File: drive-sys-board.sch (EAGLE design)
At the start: 30 parts, among them J2 APP_2POS_CONFIG12V_HORIZ, U1 OKI-78SR-5/1.5-W36HC, U2 MAX232, U3 MAX232, U4 MAX232

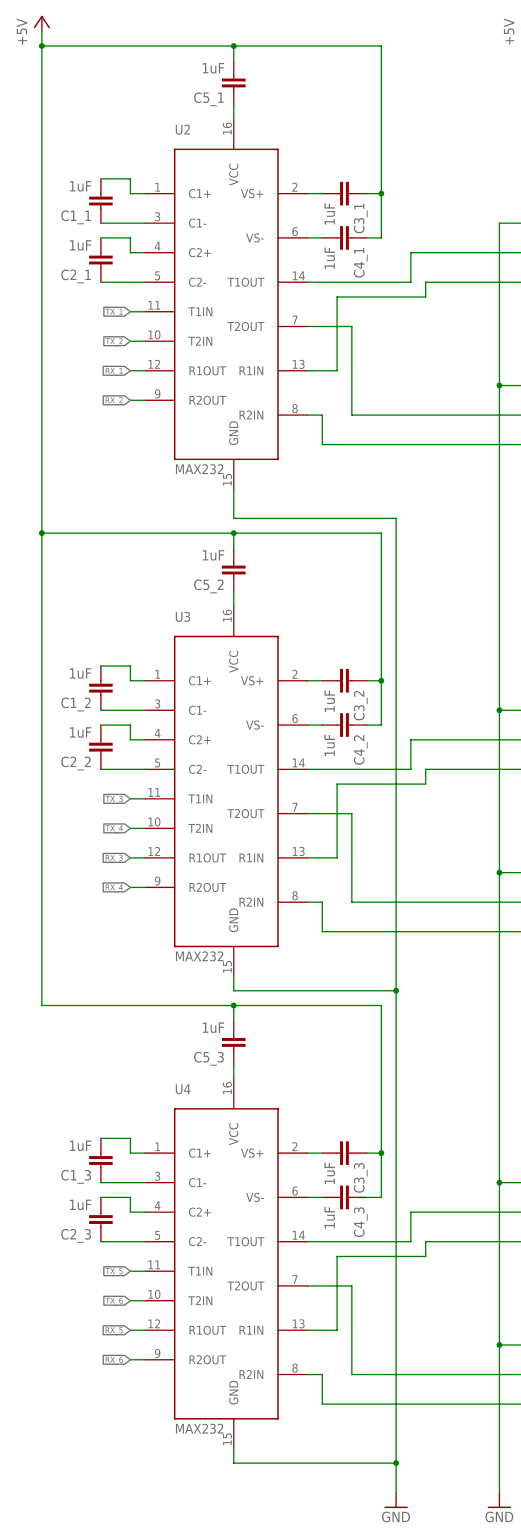
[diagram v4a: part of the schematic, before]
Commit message: Fixed RS232 chip capacitors
Several capacitors were going to Vcc when they should have been going to
Gnd
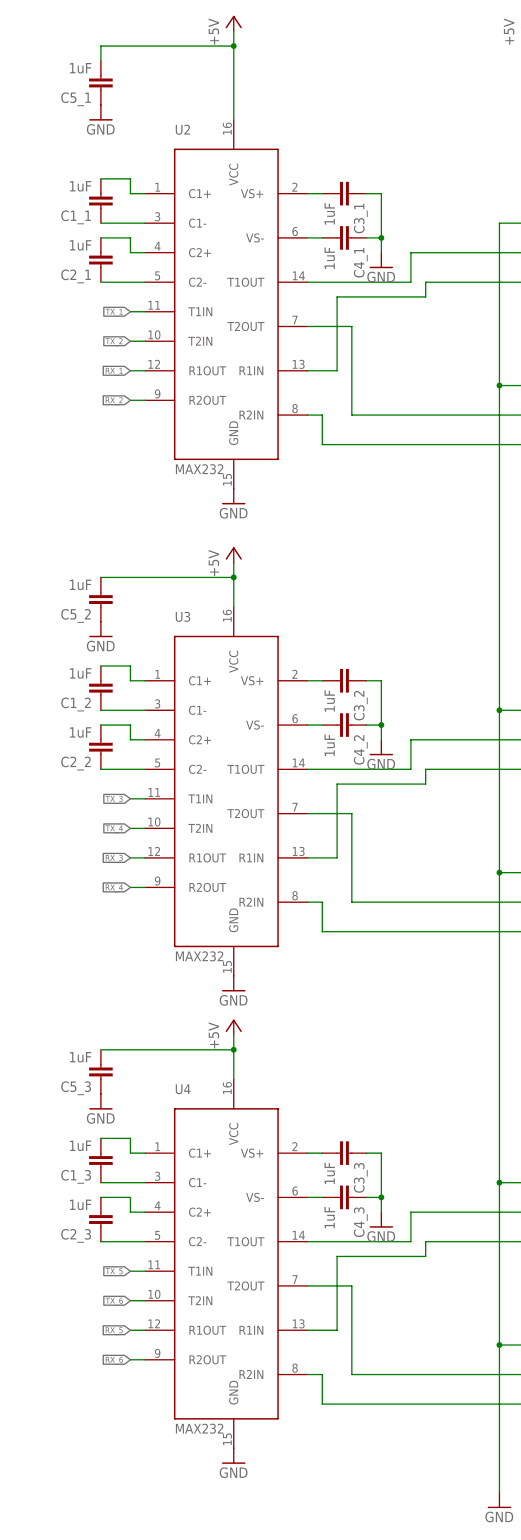
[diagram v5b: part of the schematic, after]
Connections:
- removed net N$10: C5_1.1, U2.VCC
- removed net N$17: C5_2.1, U3.VCC
- removed net N$24: C5_3.1, U4.VCC
- net +5V: now also U2.VCC, U3.VCC, U4.VCC; no longer C3_1.1, C3_2.1, C3_3.1, C4_1.1, C4_2.1, C4_3.1
- net GND: now also C3_1.1, C3_2.1, C3_3.1, C4_1.1, C4_2.1, C4_3.1, C5_1.1, C5_2.1, C5_3.1
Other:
- moved on the sheet: C5_1, C5_2, C5_3

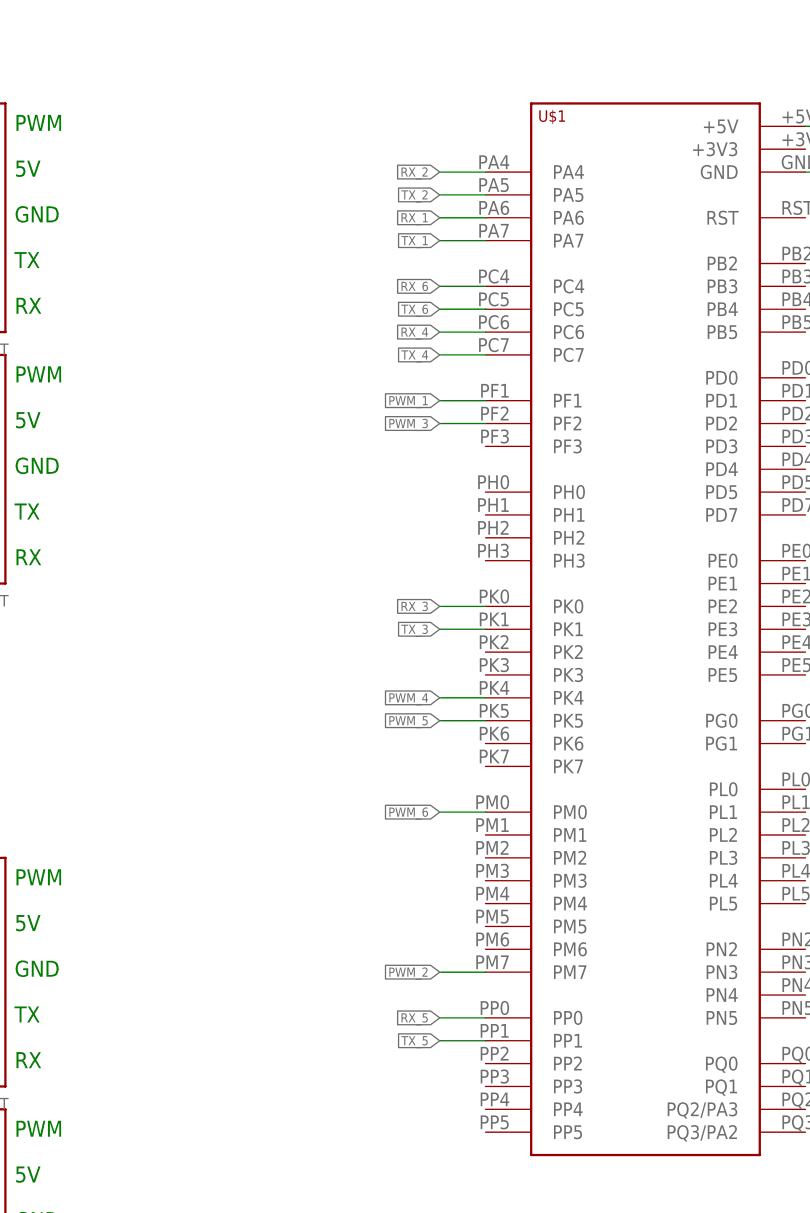
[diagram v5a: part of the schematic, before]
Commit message: Began routing traces
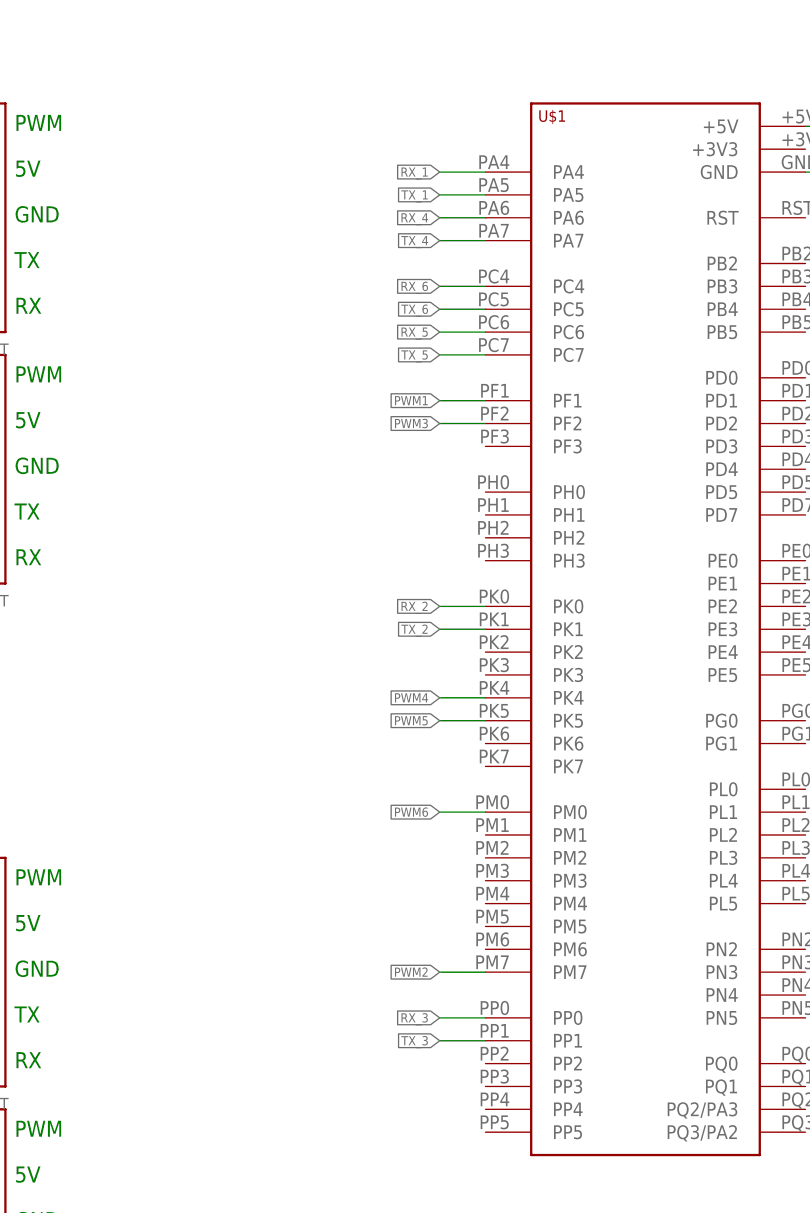
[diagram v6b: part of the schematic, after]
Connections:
- new net PWM1: U$1.PF1
- new net PWM2: U$1.PM7
- new net PWM3: U$1.PF2
- new net PWM4: U$1.PK4
- new net PWM5: U$1.PK5
- new net PWM6: U$1.PM0
- net PWM_1: no longer U$1.PF1
- net PWM_2: no longer U$1.PM7
- net PWM_3: no longer U$1.PF2
- net PWM_4: no longer U$1.PK4
- net PWM_5: no longer U$1.PK5
- net PWM_6: no longer U$1.PM0
- net RX_1: now also U$1.PA4; no longer U$1.PA6
- net RX_2: now also U$1.PK0; no longer U$1.PA4
- net RX_3: now also U$1.PP0; no longer U$1.PK0
- net RX_4: now also U$1.PA6; no longer U$1.PC6
- net RX_5: now also U$1.PC6; no longer U$1.PP0
- net TX_1: now also U$1.PA5; no longer U$1.PA7
- net TX_2: now also U$1.PK1; no longer U$1.PA5
- net TX_3: now also U$1.PP1; no longer U$1.PK1
- net TX_4: now also U$1.PA7; no longer U$1.PC7
- net TX_5: now also U$1.PC7; no longer U$1.PP1

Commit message: Updated Max232 and Tiva to Eagle libraries commit 9c171e
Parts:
- U$1: value TIVA-C-CONNECTED -> TIVA-1294; device MRDT-2015-General:TIVA-C-CONNECTED -> MRDT-Microcontrollers:TIVA-1294
- U2, U3, U4: value MAX232 -> MAX232D; device MRDT-ICs:MAX232 -> MRDT-ICs:MAX232D
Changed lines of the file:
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@@
 <?xml version="1.0" encoding="utf-8"?>
 <!DOCTYPE eagle SYSTEM "eagle.dtd">
-<eagle version="7.7.0">
+<eagle version="7.6.0">
 <drawing>
 <settings>
@@
 <part name="P+14" library="supply1" deviceset="+5V" device=""/>
 <part name="GND20" library="supply1" deviceset="GND" device=""/>
-<part name="U$1" library="MRDT-2015-General" deviceset="TIVA-C-CONNECTED" device=""/>
+<part name="U$1" library="MRDT-Microcontrollers" deviceset="TIVA-1294" device=""/>
 <part name="U1" library="MRDT-ICs" deviceset="OKI-78SR-*/1.5-W36?C" device="H" technology="5"/>
 <part name="P+1" library="supply1" deviceset="+5V" device=""/>
 <part name="J2" library="MRDT-Connectors" deviceset="APP_2POS_CONFIG" device="12V_HORIZ"/>
-<part name="U2" library="MRDT-ICs" deviceset="MAX232" device=""/>
+<part name="U2" library="MRDT-ICs" deviceset="MAX*232" device="D"/>
 <part name="H2" library="MRDT-Hardware" deviceset="MOUNTING_HOLE" device="#6"/>
 <part name="C1_1" library="SparkFun-Capacitors" deviceset="CAP" device="0805" value="1uF"/>
@@
 <part name="C4_1" library="SparkFun-Capacitors" deviceset="CAP" device="0805" value="1uF"/>
 <part name="C5_1" library="SparkFun-Capacitors" deviceset="CAP" device="0805" value="1uF"/>
-<part name="U3" library="MRDT-ICs" deviceset="MAX232" device=""/>
+<part name="U3" library="MRDT-ICs" deviceset="MAX*232" device="D"/>
 <part name="C1_2" library="SparkFun-Capacitors" deviceset="CAP" device="0805" value="1uF"/>
 <part name="C2_2" library="SparkFun-Capacitors" deviceset="CAP" device="0805" value="1uF"/>
@@
 <part name="C5_2" library="SparkFun-Capacitors" deviceset="CAP" device="0805" value="1uF"/>
 <part name="GND1" library="supply1" deviceset="GND" device=""/>
-<part name="U4" library="MRDT-ICs" deviceset="MAX232" device=""/>
+<part name="U4" library="MRDT-ICs" deviceset="MAX*232" device="D"/>
 <part name="C1_3" library="SparkFun-Capacitors" deviceset="CAP" device="0805" value="1uF"/>
 <part name="C2_3" library="SparkFun-Capacitors" deviceset="CAP" device="0805" value="1uF"/>

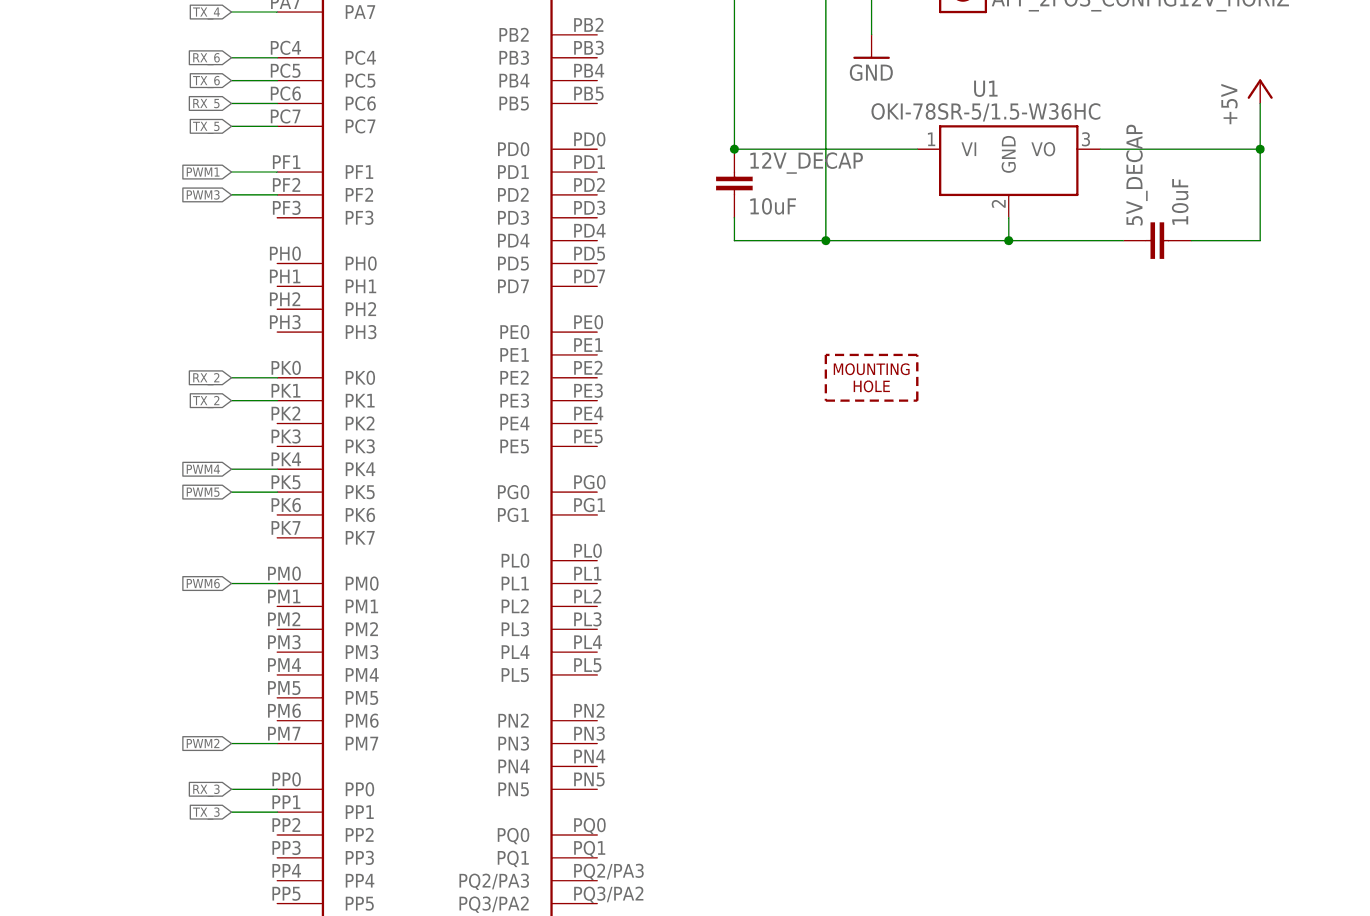
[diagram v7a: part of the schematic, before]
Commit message: Routed PWM traces and added power indicator led
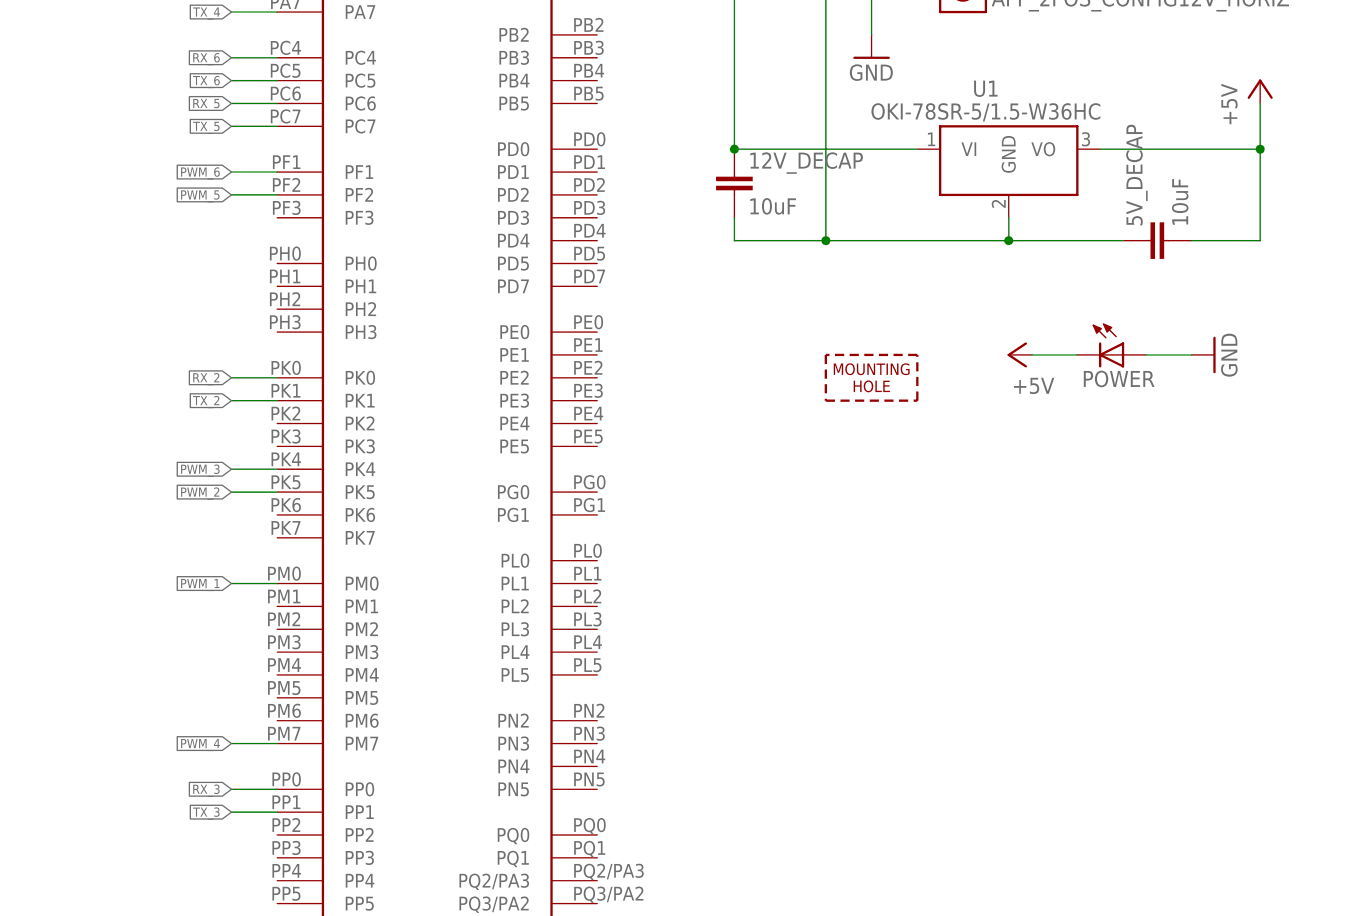
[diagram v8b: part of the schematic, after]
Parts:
- added POWER: (no value), eagle-ltspice:LED_E
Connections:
- removed net PWM1: U$1.PF1
- removed net PWM2: U$1.PM7
- removed net PWM3: U$1.PF2
- removed net PWM4: U$1.PK4
- removed net PWM5: U$1.PK5
- removed net PWM6: U$1.PM0
- net +5V: now also POWER.C
- net GND: now also POWER.A
- net PWM_1: now also U$1.PM0
- net PWM_2: now also U$1.PK5
- net PWM_3: now also U$1.PK4
- net PWM_4: now also U$1.PM7
- net PWM_5: now also U$1.PF2
- net PWM_6: now also U$1.PF1
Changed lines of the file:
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@@
 <part name="GND9" library="supply1" deviceset="GND" device=""/>
 <part name="GND10" library="supply1" deviceset="GND" device=""/>
+<part name="POWER" library="eagle-ltspice" deviceset="LED_E" device=""/>
+<part name="P+6" library="supply1" deviceset="+5V" device=""/>
+<part name="GND11" library="supply1" deviceset="GND" device=""/>
 </parts>
 <sheets>
@@
 <instance part="GND9" gate="1" x="-160.02" y="-48.26"/>
 <instance part="GND10" gate="1" x="-111.76" y="-68.58"/>
+<instance part="POWER" gate="G$1" x="88.9" y="63.5" rot="R270"/>
+<instance part="P+6" gate="1" x="76.2" y="63.5" rot="R90"/>
+<instance part="GND11" gate="1" x="99.06" y="63.5" rot="R90"/>
 </instances>
 <busses>
@@
 <junction x="-111.76" y="-63.5"/>
 </segment>
+<segment>
+<pinref part="POWER" gate="G$1" pin="A"/>
+<pinref part="GND11" gate="1" pin="GND"/>
+<wire x1="96.52" y1="63.5" x2="91.44" y2="63.5" width="0.1524" layer="91"/>
+</segment>
 </net>
 <net name="+5V" class="0">
@@
 <junction x="-137.16" y="-38.1"/>
 </segment>
+<segment>
+<pinref part="POWER" gate="G$1" pin="C"/>
+<pinref part="P+6" gate="1" pin="+5V"/>
+<wire x1="78.74" y1="63.5" x2="83.82" y2="63.5" width="0.1524" layer="91"/>
+</segment>
 </net>
 <net name="PWM_6" class="0">
@@
 <label x="-73.66" y="-78.74" size="1.016" layer="95" rot="R180" xref="yes"/>
 </segment>
+<segment>
+<pinref part="U$1" gate="G$1" pin="PF1"/>
+<wire x1="-5.08" y1="83.82" x2="-10.16" y2="83.82" width="0.1524" layer="91"/>
+<label x="-10.16" y="83.82" size="1.016" layer="95" rot="R180" xref="yes"/>
+</segment>
 </net>
 <net name="RX_1" class="0">
@@
 <label x="-73.66" y="114.3" size="1.016" layer="95" rot="R180" xref="yes"/>
 </segment>
+<segment>
+<pinref part="U$1" gate="G$1" pin="PM0"/>
+<wire x1="-5.08" y1="38.1" x2="-10.16" y2="38.1" width="0.1524" layer="91"/>
+<label x="-10.16" y="38.1" size="1.016" layer="95" rot="R180" xref="yes"/>
+</segment>
 </net>
 <net name="PWM_2" class="0">
@@
 <label x="-73.66" y="86.36" size="1.016" layer="95" rot="R180" xref="yes"/>
 </segment>
+<segment>
+<wire x1="-5.08" y1="48.26" x2="-10.16" y2="48.26" width="0.1524" layer="91"/>
+<label x="-10.16" y="48.26" size="1.016" layer="95" rot="R180" xref="yes"/>
+<pinref part="U$1" gate="G$1" pin="PK5"/>
+</segment>
 </net>
 <net name="PWM_3" class="0">
@@
 <label x="-73.66" y="2.54" size="1.016" layer="95" rot="R180" xref="yes"/>
 </segment>
+<segment>
+<wire x1="-5.08" y1="50.8" x2="-10.16" y2="50.8" width="0.1524" layer="91"/>
+<label x="-10.16" y="50.8" size="1.016" layer="95" rot="R180" xref="yes"/>
+<pinref part="U$1" gate="G$1" pin="PK4"/>
+</segment>
 </net>
 <net name="PWM_4" class="0">
@@
 <label x="-73.66" y="30.48" size="1.016" layer="95" rot="R180" xref="yes"/>
 </segment>
+<segment>
+<pinref part="U$1" gate="G$1" pin="PM7"/>
+<wire x1="-5.08" y1="20.32" x2="-10.16" y2="20.32" width="0.1524" layer="91"/>
+<label x="-10.16" y="20.32" size="1.016" layer="95" rot="R180" xref="yes"/>
+</segment>
 </net>
 <net name="PWM_5" class="0">
@@
 <wire x1="-71.12" y1="-50.8" x2="-73.66" y2="-50.8" width="0.1524" layer="91"/>
 <label x="-73.66" y="-50.8" size="1.016" layer="95" rot="R180" xref="yes"/>
+</segment>
+<segment>
+<pinref part="U$1" gate="G$1" pin="PF2"/>
+<wire x1="-5.08" y1="81.28" x2="-10.16" y2="81.28" width="0.1524" layer="91"/>
+<label x="-10.16" y="81.28" size="1.016" layer="95" rot="R180" xref="yes"/>
 </segment>
 </net>
@@
 </segment>
 </net>
-<net name="PWM1" class="0">
-<segment>
-<pinref part="U$1" gate="G$1" pin="PF1"/>
-<wire x1="-5.08" y1="83.82" x2="-10.16" y2="83.82" width="0.1524" layer="91"/>
-<label x="-10.16" y="83.82" size="1.016" layer="95" rot="R180" xref="yes"/>
-</segment>
-</net>
-<net name="PWM3" class="0">
-<segment>
-<pinref part="U$1" gate="G$1" pin="PF2"/>
-<wire x1="-5.08" y1="81.28" x2="-10.16" y2="81.28" width="0.1524" layer="91"/>
-<label x="-10.16" y="81.28" size="1.016" layer="95" rot="R180" xref="yes"/>
-</segment>
-</net>
-<net name="PWM4" class="0">
-<segment>
-<wire x1="-5.08" y1="50.8" x2="-10.16" y2="50.8" width="0.1524" layer="91"/>
-<label x="-10.16" y="50.8" size="1.016" layer="95" rot="R180" xref="yes"/>
-<pinref part="U$1" gate="G$1" pin="PK4"/>
-</segment>
-</net>
-<net name="PWM5" class="0">
-<segment>
-<wire x1="-5.08" y1="48.26" x2="-10.16" y2="48.26" width="0.1524" layer="91"/>
-<label x="-10.16" y="48.26" size="1.016" layer="95" rot="R180" xref="yes"/>
-<pinref part="U$1" gate="G$1" pin="PK5"/>
-</segment>
-</net>
-<net name="PWM2" class="0">
-<segment>
-<pinref part="U$1" gate="G$1" pin="PM7"/>
-<wire x1="-5.08" y1="20.32" x2="-10.16" y2="20.32" width="0.1524" layer="91"/>
-<label x="-10.16" y="20.32" size="1.016" layer="95" rot="R180" xref="yes"/>
-</segment>
-</net>
-<net name="PWM6" class="0">
-<segment>
-<pinref part="U$1" gate="G$1" pin="PM0"/>
-<wire x1="-5.08" y1="38.1" x2="-10.16" y2="38.1" width="0.1524" layer="91"/>
-<label x="-10.16" y="38.1" size="1.016" layer="95" rot="R180" xref="yes"/>
-</segment>
-</net>
